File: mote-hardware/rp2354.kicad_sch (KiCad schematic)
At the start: 32 parts, among them J4 SM03B-SRSS-TB, J6 Conn_01x03_Pin, SW1 SW_Push, SW2 SW_Push, U1 RP2350_60QFN, U4 RP Radio Module 2, Y1 ABM8-272-T3

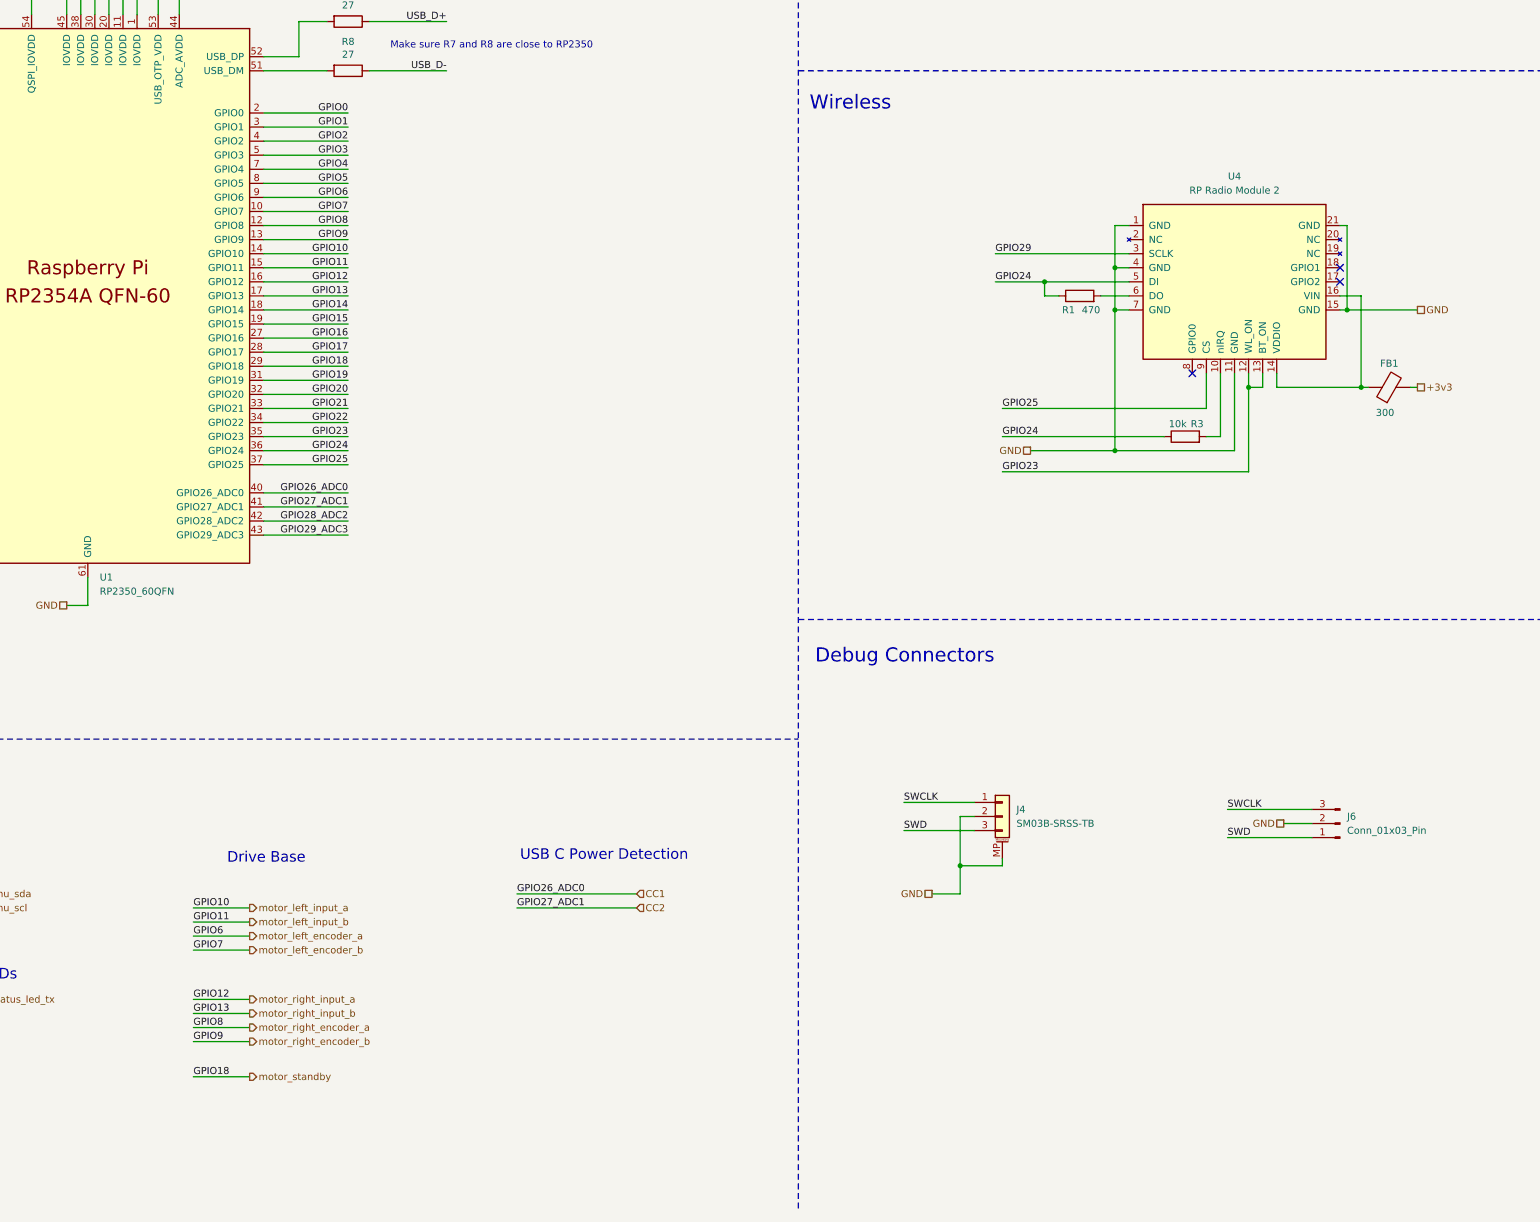
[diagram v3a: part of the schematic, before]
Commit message: Get pcb ready for first prototype order (#31)
Co-authored-by: Kyle Mui <44453997+KyleMui@users.noreply.github.com>
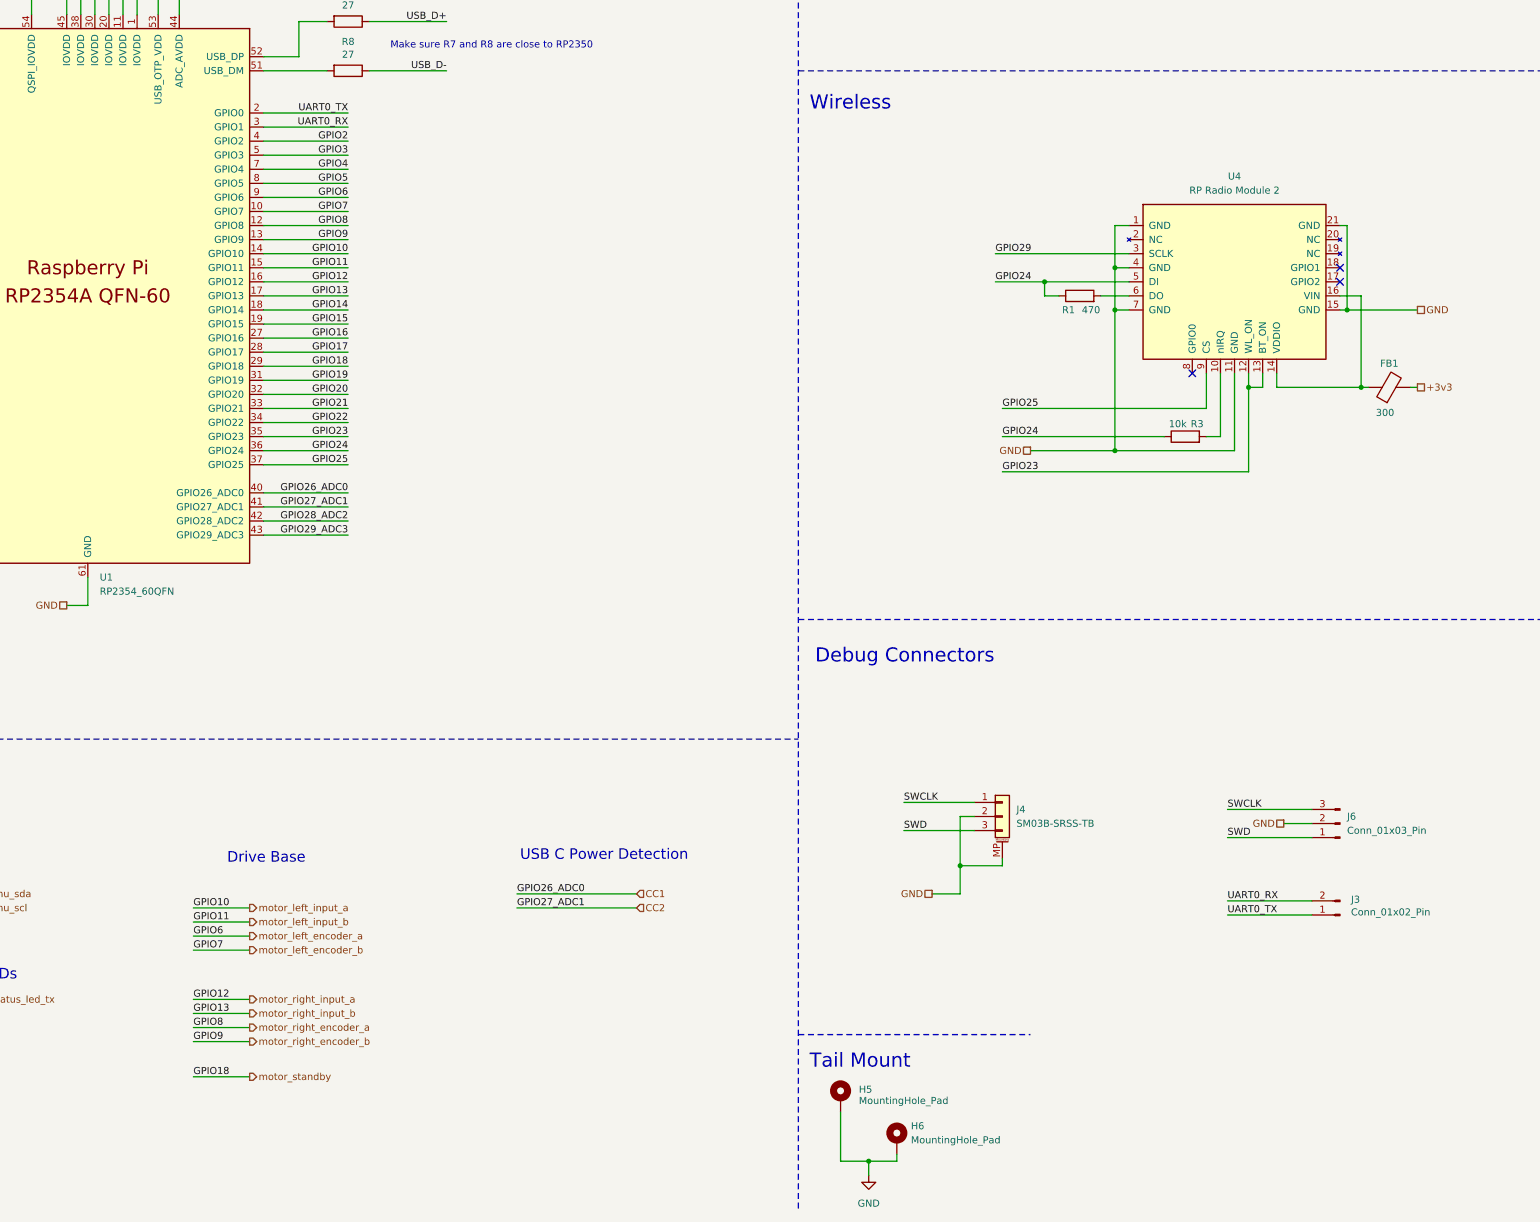
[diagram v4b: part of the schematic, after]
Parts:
- added H5, H6: MountingHole_Pad, MountingHole:MountingHole_4.3mm_M4_DIN965_Pad, symbol Mechanical:MountingHole_Pad
- added J3: Conn_01x02_Pin, Connector_PinHeader_2.54mm:PinHeader_1x02_P2.54mm_Vertical, symbol Connector:Conn_01x02_Pin
- C10, C11, C12, C13, C14, C15, C16, C17, C18, C3, C4, C8, C9: footprint Capacitor_SMD:C_0402_1005Metric -> PCM_JLCPCB:C_0402
- J4: footprint Connector_JST:JST_SH_SM03B-SRSS-TB_1x03-1MP_P1.00mm_Horizontal -> Connector_JST:JST_SH_BM03B-SRSS-TB_1x03-1MP_P1.00mm_Vertical
- R1, R2, R3, R4, R5, R6, R7, R8: footprint Resistor_SMD:R_0402_1005Metric -> PCM_JLCPCB:R_0402
- SW1, SW2: footprint Button_Switch_SMD:SW_Push_1P1T_NO_Vertical_Wuerth_434133025816 -> Button_Switch_SMD:SW_SPST_TS-1088-xR020
- U1: value RP2350_60QFN -> RP2354_60QFN
- Y1: footprint Crystal:Crystal_SMD_3225-4Pin_3.2x2.5mm -> PCM_JLCPCB:CRYSTAL-SMD_4P-L3.2-W2.5-BL
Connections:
- net GND: now also H5.1, H6.1
- net GPIO0 renamed UART0_TX
- net UART0_TX: now also J3.1 (Pin_1)
- net GPIO1 renamed UART0_RX
- net UART0_RX: now also J3.2 (Pin_2)
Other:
- note added: "Tail Mount"
- company: github.com/usedhondacivic/mote -> github.com/empriselab/mote-core

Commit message: Fix DRC warnings
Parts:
- H5, H6: now in the parts list
- J3, J6: now left out of the parts list
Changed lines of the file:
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@@
 		(unit 1)
 		(exclude_from_sim no)
-		(in_bom no)
+		(in_bom yes)
 		(on_board yes)
 		(dnp no)
@@
 		(unit 1)
 		(exclude_from_sim no)
-		(in_bom no)
+		(in_bom yes)
 		(on_board yes)
 		(dnp no)
@@
 		(unit 1)
 		(exclude_from_sim no)
-		(in_bom yes)
+		(in_bom no)
 		(on_board yes)
 		(dnp no)
@@
 		(unit 1)
 		(exclude_from_sim no)
-		(in_bom yes)
-		(on_board yes)
-		(dnp no)
+		(in_bom no)
+		(on_board yes)
+		(dnp no)

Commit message: Hardware v0.0.0 order (#36)
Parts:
- C10, C6, C7, C9: LCSC (none) -> C23733
- C11, C12, C13, C14, C15, C16, C17, C18, C8: LCSC (none) -> C1525
- C3, C4: LCSC (none) -> C1548
- FB1: LCSC (none) -> C67451
- H5, H6: LCSC (none) -> C5301776
- J3, J6: now not fitted
- J4: LCSC (none) -> C160403
- L1: LCSC (none) -> C42411119
- R1: LCSC (none) -> C25117
- R2, R4, R6: LCSC (none) -> C11702
- R3: LCSC (none) -> C25744
- R5: LCSC (none) -> C25105
- R7, R8: LCSC (none) -> C25100
- SW1, SW2: LCSC (none) -> C720477
- U1: LCSC (none) -> C41378174
- U4: now left out of the parts list
- Y1: LCSC (none) -> C20625731

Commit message: Hardware v0.1.0 updates (#52)
Addresses errata / improvements identified in
https://github.com/empriselab/mote-core/issues/37

---------

Co-authored-by: Kyle Mui <44453997+KyleMui@users.noreply.github.com>
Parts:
- removed J3: Conn_01x02_Pin, Connector_PinHeader_2.54mm:PinHeader_1x02_P2.54mm_Vertical, symbol Connector:Conn_01x02_Pin
- added D18, D19, D20, D21, D22, D23: PTVS5V0S1UR-FS, Diode_SMD:D_SOD-123, symbol Diode:PTVS5V0Z1USK
- added J5: Conn_01x03_Pin, Connector_PinHeader_2.54mm:PinHeader_1x03_P2.54mm_Vertical, symbol Connector:Conn_01x03_Pin
- C10, C11, C12, C13, C14, C15, C16, C17, C18, C3, C4, C6, C7, C8, C9, FB1, R1, R2, R3, R4, R5, R6, R7, R8, SW1, SW2, U1, Y1: JLCPCB_CORRECTION (none) -> 0; 0; 0
- H5, H6: footprint MountingHole:MountingHole_4.3mm_M4_DIN965_Pad -> MountingHole:MountingHole_4.3mm_M4_DIN965_Pad_TopOnly; JLCPCB_CORRECTION (none) -> 0; 0; 0
- J4: JLCPCB_CORRECTION (none) -> 0; 0; 180; LCSC C160403 -> C160389
- L1: JLCPCB_CORRECTION (none) -> 0; 0; 180
- U4: JLCPCB_CORRECTION (none) -> 0; 0; 0; LCSC (none) -> C49302697; now in the parts list
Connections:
- net GPIO29 is gone; now on net GPIO29_ADC3: U4.3 (SCLK)
- net GND: now also J6.1 (Pin_1), D18.2 (A), D19.2 (A), D20.2 (A), D21.2 (A), D22.2 (A), D23.2 (A), J5.1 (Pin_1); no longer J6.2 (Pin_2)
- net RUN: now also D22.1 (K)
- net SWCLK: now also D18.1 (K)
- net SWD: now also J6.2 (Pin_2), D19.1 (K); no longer J6.1 (Pin_1)
- net UART0_RX: now also D20.1 (K), J5.3 (Pin_3)
- net UART0_TX: now also D21.1 (K), J5.2 (Pin_2)
- net ~{USB_BOOT}: now also D23.1 (K)
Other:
- note added: "ESD Protection"
- note added: "SWD 2.5mm pin header"
- note added: "SWD JST SH 1.00 mm"
- note added: "UART 2.5mm pin header"
- moved on the sheet: H5, H6, J4, J6
